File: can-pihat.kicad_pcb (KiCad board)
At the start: 2 copper layers, 0 parts

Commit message: Initial version of Can-PiHAT PCB.
This commit contains the 1st version
of the board pcb. The edges are based
on the measurements from raspberry pi
hat mechanical spec:

https://tinyurl.com/hc8a3t8

Imported netlist and assigned drills
to locations based on spec.
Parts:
- added 10k1: R, Resistors_SMD:R_0805, F.Cu at (299.2, 171.6)
- added 10k2: R, Resistors_SMD:R_0805, F.Cu at (264.5, 194.2)
- added C1: 0.1uF, Capacitors_SMD:C_0805, F.Cu at (246.1, 174.7)
- added C10: 100pF, Capacitors_SMD:C_0805, F.Cu at (317.1, 168.0)
- added C11: 0.1uF, Capacitors_SMD:C_0805, F.Cu at (292.3, 190.3)
- added C12: 100pf, Capacitors_SMD:C_0805, F.Cu at (259.7, 200.5)
- added C13: 100nf, Capacitors_SMD:C_0805, F.Cu at (260.1, 194.2)
- added C14: 22pf, Capacitors_SMD:C_0805, F.Cu at (255.3, 197.1)
- added C15: 22pf, Capacitors_SMD:C_0805, F.Cu at (263.4, 188.0)
- added C2: 0.1uF, Capacitors_SMD:C_0805, F.Cu at (241.5, 175.6)
- added C3: 0.1uF, Capacitors_SMD:C_0805, F.Cu at (261.3, 169.3)
- added C4: 0.1uF, Capacitors_SMD:C_0805, F.Cu at (271.6, 169.0)
- added C5: 100pf, Capacitors_SMD:C_0805, F.Cu at (312.3, 163.7)
- added C6: 100pf, Capacitors_SMD:C_0805, F.Cu at (317.1, 161.7)
- added C7: 22pf, Capacitors_SMD:C_0805, F.Cu at (322.3, 154.6)
- added C8: 22pf, Capacitors_SMD:C_0805, F.Cu at (308.0, 169.9)
- added C9: 100pF, Capacitors_SMD:C_0805, F.Cu at (326.9, 154.6)
- added H1: DRILL, FootPrints:drill3mm, F.Cu at (111.0, 123.0)
- added H2: DRILL, FootPrints:drill3mm, F.Cu at (169.0, 74.0)
- added H3: DRILL, FootPrints:drill3mm, F.Cu at (169.0, 123.0)
- added H4: DRILL, FootPrints:drill3mm, F.Cu at (111.0, 74.0)
- added H5: DRILL, FootPrints:ovaldrill, F.Cu at (156.0, 115.0)
- added IC1: CAT24C32WI-GT3, FootPrints:SO8E, F.Cu at (296.0, 183.6)
- added L1: 47uH, Choke_SMD:Choke_SMD_1206_Standard, F.Cu at (317.5, 155.0)
- added P1: CONN_20X2, FootPrints:PIN_ARRAY_20X2, F.Cu at (140.0, 74.0)
- added P2: CONN_01X03, Terminal_Blocks:TerminalBlock_Pheonix_PT-3.5mm_3pol, F.Cu at (241.5, 164.6)
- added R1: 10k, Resistors_SMD:R_0805, F.Cu at (311.9, 169.9)
- added R2: 10k, Resistors_SMD:R_0805, F.Cu at (322.1, 160.8)
- added R3: 2.7k, Resistors_SMD:R_0805, F.Cu at (325.8, 160.8)
- added R4: 6.49k, Resistors_SMD:R_0805, F.Cu at (331.6, 154.6)
- added R5: 1k, Resistors_SMD:R_0805, F.Cu at (304.2, 169.5)
- added R7: 3.9K, Resistors_SMD:R_0805, F.Cu at (303.9, 183.1)
- added R8: 3.9K, Resistors_SMD:R_0805, F.Cu at (296.4, 190.3)
- added R9: 120, Resistors_SMD:R_0805, F.Cu at (259.5, 188.0)
- added U1: TXB0108, Housings_SSOP:TSSOP-20_4.4x6.5mm_Pitch0.65mm, F.Cu at (254.9, 164.6)
- added U2: TXB0102, FootPrints:8-VFSOP, F.Cu at (261.8, 162.9)
- added U3: NCV7356, SMD_Packages:SOIC-8-N, F.Cu at (293.6, 172.5)
- added U4: MCP2515, Housings_SOIC:SOIC-20W_7.5x12.8mm_Pitch1.27mm, F.Cu at (296.2, 160.0)
- added U5: PESD1LIN, Diodes_SMD:D_SOD-323, F.Cu at (306.0, 163.4)
- added U6: MCP2515, Housings_SOIC:SOIC-20W_7.5x12.8mm_Pitch1.27mm, F.Cu at (239.2, 193.4)
- added U7: TJA1050, Housings_SOIC:SOIC-8_3.9x4.9mm_Pitch1.27mm, F.Cu at (249.3, 198.5)
- added Y1: 8Mhz, Crystals:Crystal_HC49-U_Vertical, F.Cu at (306.1, 156.0)
- added Y2: 8Mhz, Crystals:Crystal_HC49-U_Vertical, F.Cu at (249.1, 189.4)
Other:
- board outline added: 256.5 x 71.4 mm
- rule trace_min: 0.2 -> 0.254
- rule via_min_drill: 0.3 -> 0.381
- rule via_min_size: 0.4 -> 0.889

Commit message: Blank PCB Board
This commit in contains an empty pcb board with raspberry
pi hat dimensions
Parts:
- removed 10k1, 10k2: R, Resistors_SMD:R_0805
- removed C1, C11, C2, C3, C4: 0.1uF, Capacitors_SMD:C_0805
- removed C10, C9: 100pF, Capacitors_SMD:C_0805
- removed C12, C5, C6: 100pf, Capacitors_SMD:C_0805
- removed C13: 100nf, Capacitors_SMD:C_0805
- removed C14, C15, C7, C8: 22pf, Capacitors_SMD:C_0805
- removed IC1: CAT24C32WI-GT3, FootPrints:SO8E
- removed L1: 47uH, Choke_SMD:Choke_SMD_1206_Standard
- removed P1: CONN_20X2, FootPrints:PIN_ARRAY_20X2
- removed P2: CONN_01X03, Terminal_Blocks:TerminalBlock_Pheonix_PT-3.5mm_3pol
- removed R1, R2: 10k, Resistors_SMD:R_0805
- removed R3: 2.7k, Resistors_SMD:R_0805
- removed R4: 6.49k, Resistors_SMD:R_0805
- removed R5: 1k, Resistors_SMD:R_0805
- removed R7, R8: 3.9K, Resistors_SMD:R_0805
- removed R9: 120, Resistors_SMD:R_0805
- removed U1: TXB0108, Housings_SSOP:TSSOP-20_4.4x6.5mm_Pitch0.65mm
- removed U2: TXB0102, FootPrints:8-VFSOP
- removed U3: NCV7356, SMD_Packages:SOIC-8-N
- removed U4, U6: MCP2515, Housings_SOIC:SOIC-20W_7.5x12.8mm_Pitch1.27mm
- removed U5: PESD1LIN, Diodes_SMD:D_SOD-323
- removed U7: TJA1050, Housings_SOIC:SOIC-8_3.9x4.9mm_Pitch1.27mm
- removed Y1, Y2: 8Mhz, Crystals:Crystal_HC49-U_Vertical
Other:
- board size 256.5 x 71.4 mm -> 65 x 56 mm

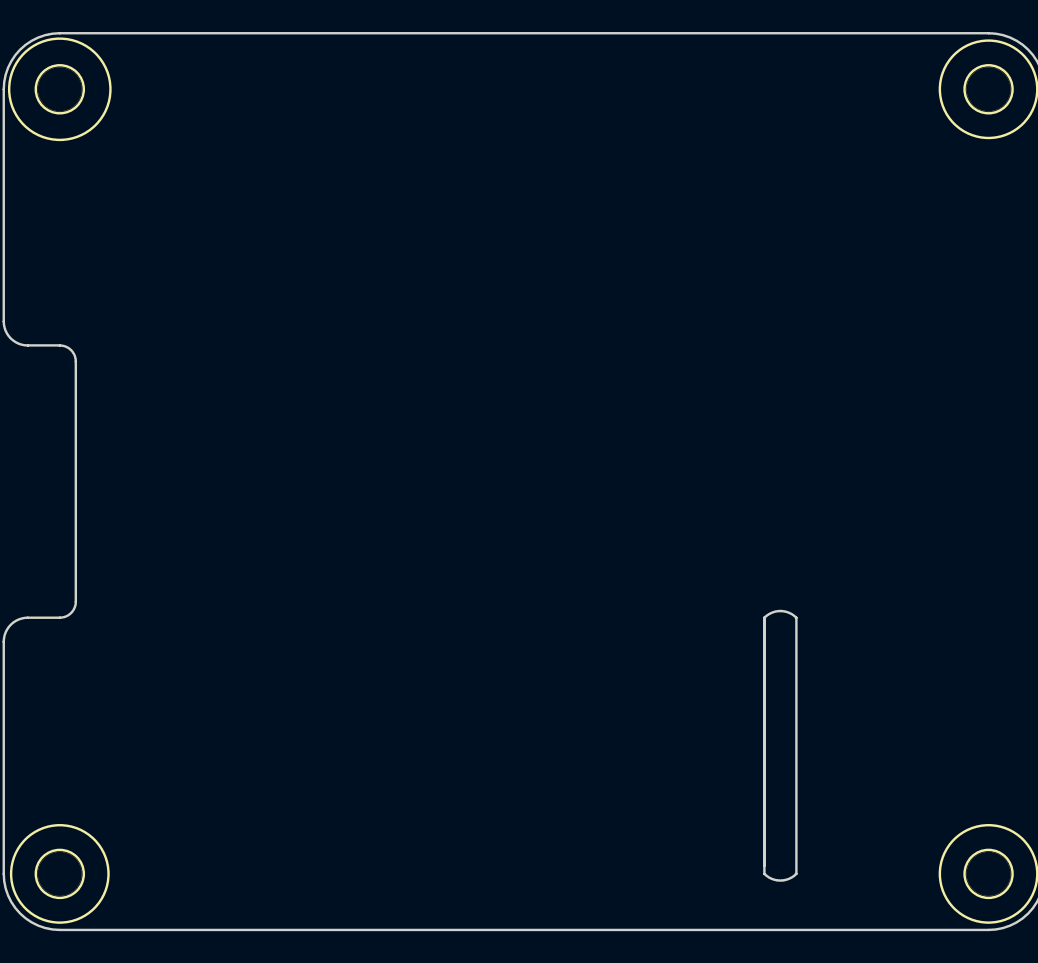
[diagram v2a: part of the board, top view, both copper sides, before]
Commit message: This is an initial attempt to board layout and trace routing. The board uses two layers top side plane is 5v and bottom plane is ground. Next will be figure out better trace routes.
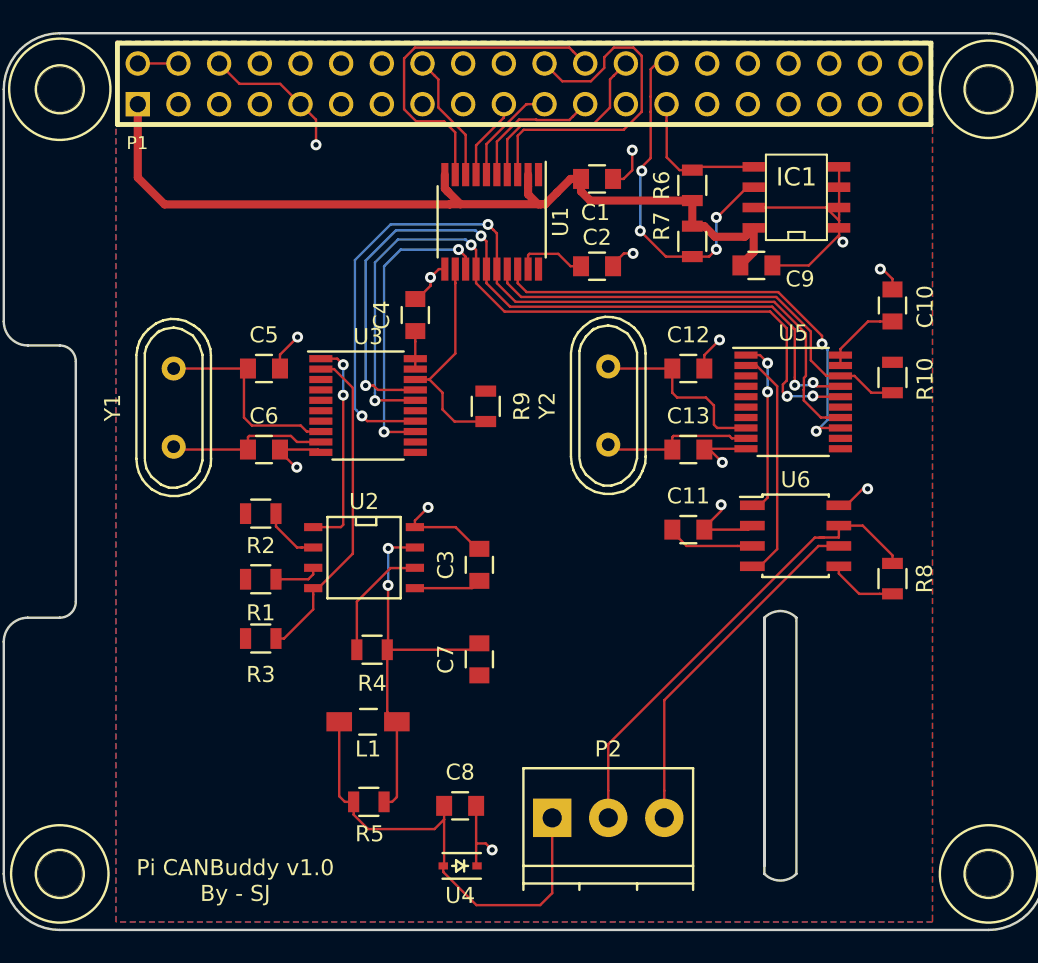
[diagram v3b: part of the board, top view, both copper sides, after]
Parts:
- added C1: 0.1uF, Capacitors_SMD:C_0805, F.Cu at (144.6, 79.6)
- added C10: 100pf, Capacitors_SMD:C_0805, F.Cu at (163.0, 87.5)
- added C11: 100nf, Capacitors_SMD:C_0805, F.Cu at (150.2, 101.5)
- added C12: 22pf, Capacitors_SMD:C_0805, F.Cu at (150.2, 91.4)
- added C13: 22pf, Capacitors_SMD:C_0805, F.Cu at (150.2, 96.5)
- added C2: 0.1uF, Capacitors_SMD:C_0805, F.Cu at (144.6, 85.0)
- added C3: 100pf, Capacitors_SMD:C_0805, F.Cu at (137.2, 103.7)
- added C4: 100pf, Capacitors_SMD:C_0805, F.Cu at (133.2, 88.1)
- added C5: 22pf, Capacitors_SMD:C_0805, F.Cu at (123.8, 91.4)
- added C6: 22pf, Capacitors_SMD:C_0805, F.Cu at (123.8, 96.5)
- added C7: 100pF, Capacitors_SMD:C_0805, F.Cu at (137.2, 109.6)
- added C8: 100pF, Capacitors_SMD:C_0805, F.Cu at (136.0, 118.8)
- added C9: 0.1uF, Capacitors_SMD:C_0805, F.Cu at (154.5, 85.0)
- added IC1: CAT24C32WI-GT3, FootPrints:SO8E, F.Cu at (157.0, 80.8)
- added L1: 47uH, Choke_SMD:Choke_SMD_1206_Standard, F.Cu at (130.2, 113.5)
- added P1: CONN_20X2, FootPrints:PIN_ARRAY_20X2, F.Cu at (140.0, 73.7)
- added P2: CONN_01X03, Terminal_Blocks:TerminalBlock_Pheonix_PT-3.5mm_3pol, F.Cu at (141.8, 119.5)
- added R1: 10k, Resistors_SMD:R_0805, F.Cu at (123.5, 104.6)
- added R10: 10k, Resistors_SMD:R_0805, F.Cu at (163.0, 92.0)
- added R2: 10k, Resistors_SMD:R_0805, F.Cu at (123.5, 100.5)
- added R3: 2.7k, Resistors_SMD:R_0805, F.Cu at (123.5, 108.3)
- added R4: 6.49k, Resistors_SMD:R_0805, F.Cu at (130.5, 109.0)
- added R5: 1k, Resistors_SMD:R_0805, F.Cu at (130.3, 118.5)
- added R6: 3.9K, Resistors_SMD:R_0805, F.Cu at (150.5, 80.0)
- added R7: 3.9K, Resistors_SMD:R_0805, F.Cu at (150.5, 83.5)
- added R8: 120, Resistors_SMD:R_0805, F.Cu at (163.0, 104.6)
- added R9: 10k, Resistors_SMD:R_0805, F.Cu at (137.6, 93.8)
- added U1: TXB0108, Housings_SSOP:TSSOP-20_4.4x6.5mm_Pitch0.65mm, F.Cu at (138.0, 82.3)
- added U2: NCV7356, SMD_Packages:SOIC-8-N, F.Cu at (130.0, 103.2)
- added U3: MCP2515, Housings_SSOP:TSSOP-20_4.4x6.5mm_Pitch0.65mm, F.Cu at (130.2, 93.8)
- added U4: PESD1LIN, Diodes_SMD:SOD-323, F.Cu at (136.0, 122.5)
- added U5: MCP2515, Housings_SSOP:TSSOP-20_4.4x6.5mm_Pitch0.65mm, F.Cu at (156.8, 93.5)
- added U6: TJA1050, Housings_SOIC:SOIC-8_3.9x4.9mm_Pitch1.27mm, F.Cu at (156.9, 101.9)
- added Y1: 8Mhz, Crystals:Crystal_HC49-U_Vertical, F.Cu at (118.1, 93.9)
- added Y2: 8Mhz, Crystals:Crystal_HC49-U_Vertical, F.Cu at (145.2, 93.8)
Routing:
- net GND: track 0.00 -> 64.8 mm, vias 0 -> 14
- net SPI_CLK: track 0.00 -> 54.1 mm, vias 0 -> 2
- net +3V3: track 0.00 -> 54.0 mm
- net SPI_MISO: track 0.00 -> 49.2 mm, vias 0 -> 4
- net SPI_MOSI: track 0.00 -> 48.8 mm, vias 0 -> 4
- net HSCAN+: track 0.00 -> 29.9 mm
- net SWCAN: track 0.00 -> 29.6 mm
- net HSCAN_INT: track 0.00 -> 29.2 mm, vias 0 -> 2
- net +5V: track 0.00 -> 29.0 mm
- net HSCAN_CS: track 0.00 -> 28.8 mm
- net Net-(C7-Pad2): track 0.00 -> 24.6 mm, vias 0 -> 2
- net ID_SC: track 0.00 -> 22.6 mm, vias 0 -> 4
- net PI_HSCAN_INT: track 0.00 -> 22.3 mm
- net HSCAN-: track 0.00 -> 22.2 mm
- net PI_SPI0_CE0: track 0.00 -> 21.6 mm
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- added copper zone on F.Cu, net +5V
- added copper zone on B.Cu, net GND
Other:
- net class 3v added: clearance 0.1524, trace_width 0.508, via_dia 0.6858, via_drill 0.3302
- net class 5v added: clearance 0.1524, trace_width 0.508, via_dia 0.6858, via_drill 0.3302
- net class Default: clearance 0.2 -> 0.1524; trace_width 0.25 -> 0.1524; via_dia 0.6 -> 0.6858; via_drill 0.4 -> 0.3302
- rule trace_clearance: 0.2 -> 0.1524
- rule trace_min: 0.254 -> 0.1524
- rule via_min_drill: 0.381 -> 0.3302
- rule via_min_size: 0.889 -> 0.6858
- board text added: "Pi"
- board text added: "Pi CANBuddy v1.0 By - SJ"
- board text added: "Pi CANBuddy, v1.0 By - SJ"
- board text added: "SW"

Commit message: This is the second iteration of CanPi-HAT PCB. This commit includes:
1. Fixes the corrent footprint for CAT24C32WI
2. Instead of power plain, a 5v trace is made in the bottom layer of
the pcb. This trace travels underneath most of the board to provide
power all ICs.
3. Corrected decoupling capacitor use. The power trace will now first
go to the decoupling capacitor and then to the respective IC.
4. The SPI bus traces for SWCAN is moved to top layer. This keeps it
consistent with HSWCAN layout.
5. Fixed issue in MCP2515-Crystal layout. The traces from XTAL pins of
MCP2515 to first go to the crystal and then to the caps.
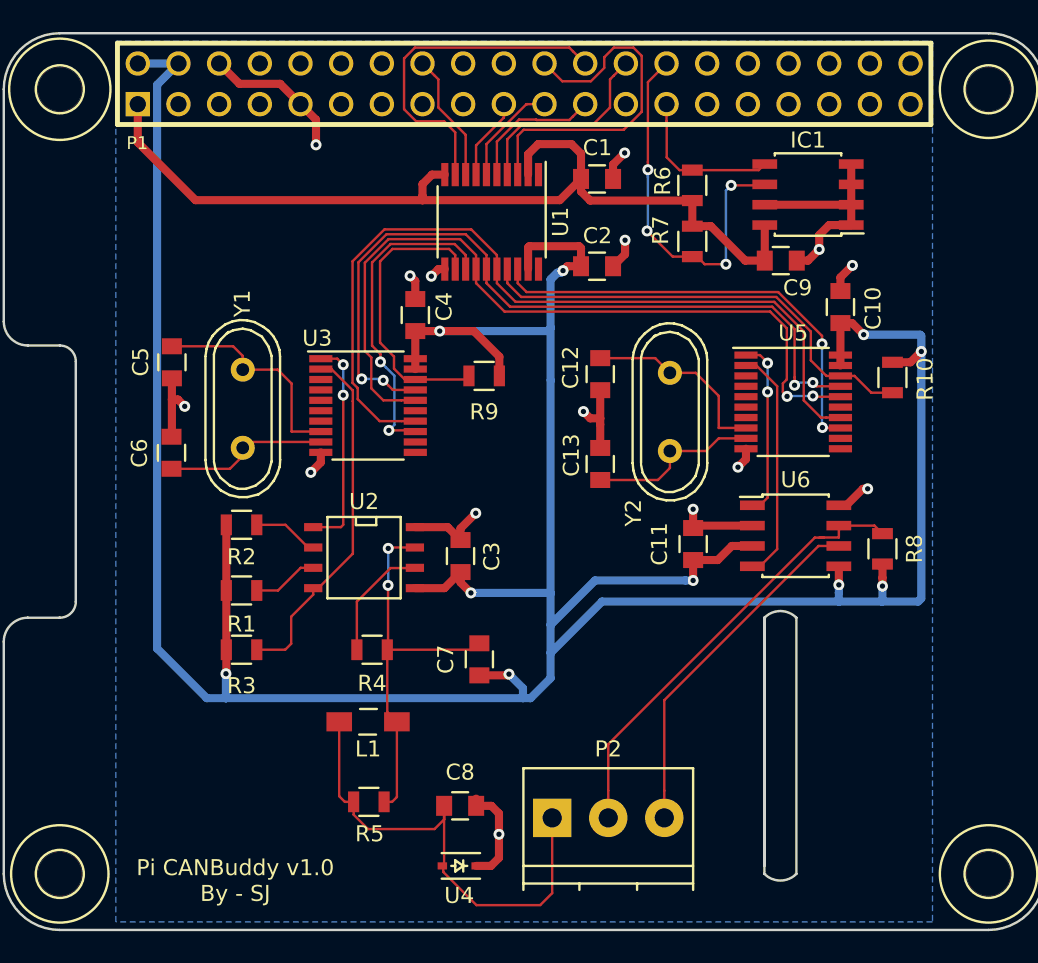
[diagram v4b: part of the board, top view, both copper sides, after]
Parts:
- IC1: footprint FootPrints:SO8E -> Housings_SOIC:SOIC-8_3.9x4.9mm_Pitch1.27mm
- moved C6 5.78 mm to (118.0, 96.7), turned to 90 degrees
- moved C5 5.76 mm to (118.0, 91.0), turned to 270 degrees
- moved C13 5.57 mm to (144.8, 97.4), turned to 90 degrees
- moved C12 5.51 mm to (144.8, 91.8), turned to 270 degrees
- moved Y1 4.32 mm to (122.4, 94.0)
- moved Y2 3.87 mm to (149.1, 94.2)
- moved C10 3.25 mm to (159.8, 87.6)
- moved R8 1.96 mm to (162.4, 102.7)
- moved R9 1.90 mm to (137.5, 91.9), turned to 180 degrees
- moved C9 1.55 mm to (156.0, 84.7)
- moved R1 1.39 mm to (122.3, 105.3)
- moved R2 1.39 mm to (122.3, 101.2)
- moved R3 1.39 mm to (122.3, 109.0)
- moved C3 1.30 mm to (136.0, 103.2)
- moved C11 0.95 mm to (150.6, 102.4), turned to 90 degrees
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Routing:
- net +5V: track 29.0 -> 213.1 mm, vias 0 -> 10
- net SWCAN_CS: track 13.7 -> 18.2 mm
- net +3V3: track 54.0 -> 58.2 mm
- net GND: track 64.8 -> 62.9 mm, vias 14 -> 15
- net SWCAN_RxD: track 20.8 -> 22.7 mm
- net ID_SC: track 22.6 -> 24.4 mm
- net HSCAN+: track 29.9 -> 28.2 mm
- net SWCAN_INT: track 18.8 -> 20.4 mm
- net SPI_CLK: track 54.1 -> 52.6 mm, vias 2 -> 0
- net Net-(C13-Pad1): track 9.60 -> 11.0 mm
- net Net-(R1-Pad1): track 3.79 -> 5.05 mm
- net HSCAN_INT: track 29.2 -> 28.1 mm
- net SWCAN: track 29.6 -> 30.6 mm
- net ID_SD: track 9.30 -> 10.2 mm
- net Net-(C5-Pad1): track 13.0 -> 13.9 mm
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- removed copper zone on F.Cu, net +5V
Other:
- net class GND added: clearance 0.1524, trace_width 0.508, via_dia 0.6858, via_drill 0.3302
